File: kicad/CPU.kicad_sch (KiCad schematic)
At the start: 45 parts, among them J1 Conn_ARM_SWD_TagConnect_TC203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, J2 Screw_Terminal_01x03, J3 Screw_Terminal_01x03, SW1 SW_Push, U7 STM32F303CBTx, U8 ATA6560-GAQW-N, Y1 8 MHz

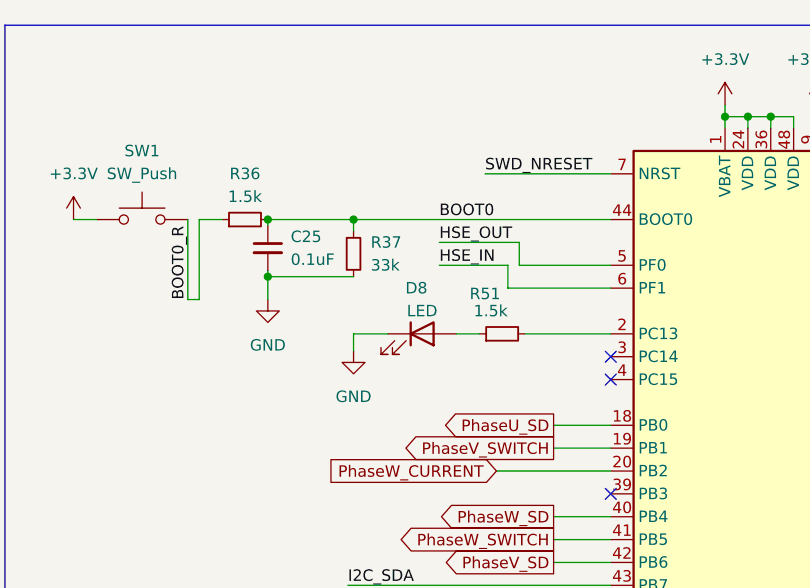
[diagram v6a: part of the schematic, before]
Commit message: finished revision 1, generate gerbers and order
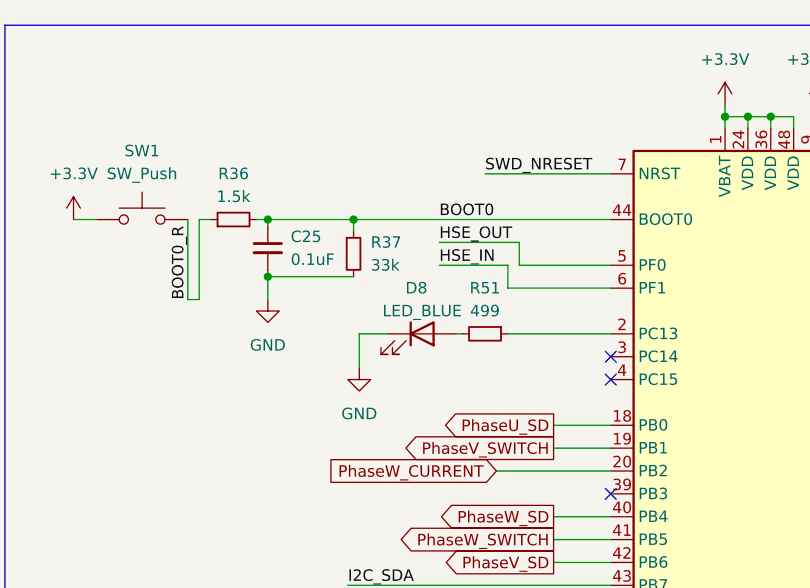
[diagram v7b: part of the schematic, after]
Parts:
- D8: value LED -> LED_BLUE; footprint LED_SMD:LED_0805_2012Metric -> LED_SMD:LED_0603_1608Metric; MFR.Part BZ-C0805-Y2-E1 -> F.0603.00026/P2-0603B1TS2-06T-001; jlcpcb C2833070 -> C7496819
- R51: value 1.5k -> 499; footprint Resistor_SMD:R_0805_2012Metric -> Resistor_SMD:R_0402_1005Metric; MFR.Part 0805W8F1501T5E -> 0402WGF4990TCE; jlcpcb C4310 -> C4125
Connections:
- net at D8.2 (A): now also R51.2; no longer R51.1
- net at U7.2 (PC13): now also R51.1; no longer R51.2
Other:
- moved on the sheet: R36
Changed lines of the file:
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@@
     (stroke (width 0) (type default))
   )
-  (wire (pts (xy 35.56 118.11) (xy 38.1 118.11))
+  (wire (pts (xy 35.56 118.11) (xy 36.83 118.11))
     (stroke (width 0) (type default))
   )
@@
     (stroke (width 0) (type default))
   )
+  (wire (pts (xy 64.77 130.81) (xy 64.135 130.81))
+    (stroke (width 0) (type default))
+  )
   (wire (pts (xy 202.565 138.43) (xy 217.805 138.43))
     (stroke (width 0) (type default))
@@
     (stroke (width 0) (type default))
   )
-  (wire (pts (xy 64.135 130.81) (xy 66.675 130.81))
-    (stroke (width 0) (type default))
-  )
   (wire (pts (xy 38.1 34.29) (xy 30.48 34.29))
     (stroke (width 0) (type default))
@@
     (stroke (width 0) (type default))
   )
-  (wire (pts (xy 52.705 130.81) (xy 56.515 130.81))
+  (wire (pts (xy 53.34 130.81) (xy 56.515 130.81))
     (stroke (width 0) (type default))
   )
@@
     (stroke (width 0) (type default))
   )
-  (wire (pts (xy 52.705 132.715) (xy 52.705 130.81))
+  (wire (pts (xy 53.34 134.62) (xy 53.34 130.81))
     (stroke (width 0) (type default))
   )
@@
     (stroke (width 0) (type default))
   )
-  (wire (pts (xy 71.755 130.81) (xy 81.28 130.81))
-    (stroke (width 0) (type default))
-  )
   (wire (pts (xy 69.85 182.88) (xy 67.31 182.88))
     (stroke (width 0) (type default))
@@
     (stroke (width 0) (type default))
   )
+  (wire (pts (xy 69.85 130.81) (xy 81.28 130.81))
+    (stroke (width 0) (type default))
+  )
   (wire (pts (xy 68.58 179.07) (xy 66.04 179.07))
     (stroke (width 0) (type default))
@@
   )
   (wire (pts (xy 238.125 132.08) (xy 238.125 140.97))
+    (stroke (width 0) (type default))
+  )
+  (wire (pts (xy 41.91 118.11) (xy 43.18 118.11))
     (stroke (width 0) (type default))
   )
@@
       (effects (font (size 1.27 1.27)))
     )
-    (property "Value" "LED" (at 60.325 128.27 0)
-      (effects (font (size 1.27 1.27)))
-    )
-    (property "Footprint" "LED_SMD:LED_0805_2012Metric" (at 60.325 130.81 0)
-      (effects (font (size 1.27 1.27)) hide)
-    )
-    (property "Datasheet" "https://wmsc.lcsc.com/wmsc/upload/file/pdf/v2/lcsc/2106081832_baizou-BZ-C0805-Y2-E1_C2833070.pdf" (at 60.325 130.81 0)
-      (effects (font (size 1.27 1.27)) hide)
-    )
-    (property "jlcpcb" "C2833070" (at 60.325 130.81 0)
-      (effects (font (size 1.27 1.27)) hide)
-    )
-    (property "MFR.Part" "BZ-C0805-Y2-E1" (at 60.325 130.81 0)
+    (property "Value" "LED_BLUE" (at 60.325 128.27 0)
+      (effects (font (size 1.27 1.27)))
+    )
+    (property "Footprint" "LED_SMD:LED_0603_1608Metric" (at 60.325 130.81 0)
+      (effects (font (size 1.27 1.27)) hide)
+    )
+    (property "Datasheet" "https://wmsc.lcsc.com/wmsc/upload/file/pdf/v2/lcsc/2308091127_TUOZHAN-F-0603-00026-P2-0603B1TS2-06T-001_C7496819.pdf" (at 60.325 130.81 0)
+      (effects (font (size 1.27 1.27)) hide)
+    )
+    (property "jlcpcb" "C7496819" (at 60.325 130.81 0)
+      (effects (font (size 1.27 1.27)) hide)
+    )
+    (property "MFR.Part" "F.0603.00026/P2-0603B1TS2-06T-001" (at 60.325 130.81 0)
       (effects (font (size 1.27 1.27)) hide)
     )
@@
     )
   )
+  (symbol (lib_id "power:GND") (at 53.34 134.62 0) (unit 1)
+    (in_bom yes) (on_board yes) (dnp no) (fields_autoplaced)
+    (property "Reference" "#PWR068" (at 53.34 140.97 0)
+      (effects (font (size 1.27 1.27)) hide)
+    )
+    (property "Value" "GND" (at 53.34 139.7 0)
+      (effects (font (size 1.27 1.27)))
+    )
+    (property "Footprint" "" (at 53.34 134.62 0)
+      (effects (font (size 1.27 1.27)) hide)
+    )
+    (property "Datasheet" "" (at 53.34 134.62 0)
+      (effects (font (size 1.27 1.27)) hide)
+    )
+    (pin "1")
+    (instances
+      (project "bldc_project"
+        (path "/91e2f46a-700b-4d7a-a06a-22469f63223f/7eb1e86b-8a48-408f-b231-0c52f4ea1971"
+          (reference "#PWR068") (unit 1)
+        )
+      )
+    )
+  )
   (symbol (lib_id "Connector:Screw_Terminal_01x03") (at 263.525 132.08 0) (unit 1)
     (in_bom yes) (on_board yes) (dnp no)
@@
     )
   )
-  (symbol (lib_id "Device:R_Small") (at 40.64 118.11 90) (unit 1)
-    (in_bom yes) (on_board yes) (dnp no) (fields_autoplaced)
-    (property "Reference" "R36" (at 40.64 113.03 90)
-      (effects (font (size 1.27 1.27)))
-    )
-    (property "Value" "1.5k" (at 40.64 115.57 90)
-      (effects (font (size 1.27 1.27)))
-    )
-    (property "Footprint" "Resistor_SMD:R_0805_2012Metric" (at 40.64 118.11 0)
-      (effects (font (size 1.27 1.27)) hide)
-    )
-    (property "Datasheet" "https://wmsc.lcsc.com/wmsc/upload/file/pdf/v2/lcsc/2206010216_UNI-ROYAL-Uniroyal-Elec-0805W8F1501T5E_C4310.pdf" (at 40.64 118.11 0)
-      (effects (font (size 1.27 1.27)) hide)
-    )
-    (property "jlcpcb" "C4310" (at 40.64 118.11 0)
-      (effects (font (size 1.27 1.27)) hide)
-    )
-    (property "MFR.Part" "0805W8F1501T5E" (at 40.64 118.11 0)
+  (symbol (lib_id "Device:R_Small") (at 39.37 118.11 90) (unit 1)
+    (in_bom yes) (on_board yes) (dnp no) (fields_autoplaced)
+    (property "Reference" "R36" (at 39.37 113.03 90)
+      (effects (font (size 1.27 1.27)))
+    )
+    (property "Value" "1.5k" (at 39.37 115.57 90)
+      (effects (font (size 1.27 1.27)))
+    )
+    (property "Footprint" "Resistor_SMD:R_0805_2012Metric" (at 39.37 118.11 0)
+      (effects (font (size 1.27 1.27)) hide)
+    )
+    (property "Datasheet" "https://wmsc.lcsc.com/wmsc/upload/file/pdf/v2/lcsc/2206010216_UNI-ROYAL-Uniroyal-Elec-0805W8F1501T5E_C4310.pdf" (at 39.37 118.11 0)
+      (effects (font (size 1.27 1.27)) hide)
+    )
+    (property "jlcpcb" "C4310" (at 39.37 118.11 0)
+      (effects (font (size 1.27 1.27)) hide)
+    )
+    (property "MFR.Part" "0805W8F1501T5E" (at 39.37 118.11 0)
       (effects (font (size 1.27 1.27)) hide)
     )
@@
     )
   )
+  (symbol (lib_id "Device:R_Small") (at 67.31 130.81 270) (unit 1)
+    (in_bom yes) (on_board yes) (dnp no) (fields_autoplaced)
+    (property "Reference" "R51" (at 67.31 125.73 90)
+      (effects (font (size 1.27 1.27)))
+    )
+    (property "Value" "499" (at 67.31 128.27 90)
+      (effects (font (size 1.27 1.27)))
+    )
+    (property "Footprint" "Resistor_SMD:R_0402_1005Metric" (at 67.31 130.81 0)
+      (effects (font (size 1.27 1.27)) hide)
+    )
+    (property "Datasheet" "https://wmsc.lcsc.com/wmsc/upload/file/pdf/v2/lcsc/2206010216_UNI-ROYAL-Uniroyal-Elec-0805W8F1501T5E_C4310.pdf" (at 67.31 130.81 0)
+      (effects (font (size 1.27 1.27)) hide)
+    )
+    (property "jlcpcb" "C4125" (at 67.31 130.81 0)
+      (effects (font (size 1.27 1.27)) hide)
+    )
+    (property "MFR.Part" "0402WGF4990TCE" (at 67.31 130.81 0)
+      (effects (font (size 1.27 1.27)) hide)
+    )
+    (pin "2")
+    (pin "1")
+    (instances
+      (project "bldc_project"
+        (path "/91e2f46a-700b-4d7a-a06a-22469f63223f/7eb1e86b-8a48-408f-b231-0c52f4ea1971"
+          (reference "R51") (unit 1)
+        )
+      )
+    )
+  )
   (symbol (lib_id "Connector:Conn_ARM_SWD_TagConnect_TC2030-NL") (at 139.7 38.1 180) (unit 1)
     (in_bom no) (on_board yes) (dnp no)
@@
         )
       )
-    )
-  )
-  (symbol (lib_id "Device:R_Small") (at 69.215 130.81 90) (unit 1)
-    (in_bom yes) (on_board yes) (dnp no)
-    (property "Reference" "R51" (at 67.31 126.365 90)
-      (effects (font (size 1.27 1.27)))
-    )
-    (property "Value" "1.5k" (at 67.945 128.27 90)
-      (effects (font (size 1.27 1.27)))
-    )
-    (property "Footprint" "Resistor_SMD:R_0805_2012Metric" (at 69.215 130.81 0)
-      (effects (font (size 1.27 1.27)) hide)
-    )
-    (property "Datasheet" "https://wmsc.lcsc.com/wmsc/upload/file/pdf/v2/lcsc/2206010216_UNI-ROYAL-Uniroyal-Elec-0805W8F1501T5E_C4310.pdf" (at 69.215 130.81 0)
-      (effects (font (size 1.27 1.27)) hide)
-    )
-    (property "jlcpcb" "C4310" (at 69.215 130.81 0)
-      (effects (font (size 1.27 1.27)) hide)
-    )
-    (property "MFR.Part" "0805W8F1501T5E" (at 69.215 130.81 0)
-      (effects (font (size 1.27 1.27)) hide)
-    )
-    (pin "2")
-    (pin "1")
-    (instances
-      (project "bldc_project"
-        (path "/91e2f46a-700b-4d7a-a06a-22469f63223f/7eb1e86b-8a48-408f-b231-0c52f4ea1971"
-          (reference "R51") (unit 1)
-        )
-      )
-    )
-  )
-  (symbol (lib_id "OLIMEX_Power:GND") (at 52.705 132.715 0) (unit 1)
-    (in_bom yes) (on_board yes) (dnp no) (fields_autoplaced)
-    (property "Reference" "#PWR068" (at 52.705 139.065 0)
-      (effects (font (size 1.27 1.27)) hide)
-    )
-    (property "Value" "GND" (at 52.705 137.795 0)
-      (effects (font (size 1.27 1.27)))
-    )
-    (property "Footprint" "" (at 52.705 132.715 0)
-      (effects (font (size 1.524 1.524)))
-    )
-    (property "Datasheet" "" (at 52.705 132.715 0)
-      (effects (font (size 1.524 1.524)))
-    )
-    (pin "1")
-    (instances
-      (project "bldc_project"
-        (path "/91e2f46a-700b-4d7a-a06a-22469f63223f/7eb1e86b-8a48-408f-b231-0c52f4ea1971"
-          (reference "#PWR068") (unit 1)
-        )
-      )
